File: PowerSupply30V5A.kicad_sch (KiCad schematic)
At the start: 110 parts, among them IC1 MC7805BDTRKG, IC2 MC7815BDTRKG, IC3 MC7915BD2TR4G, IC4 MC7815BDTRKG, IC5 MC7812BDTRKG, IC6 MC7805BDTRKG, IC7 MC7915BD2TR4G, IC9 MC7812BDTRKG, J1 1017503, J11 1017503, J2 1017503, J3 76825-0004, J4 39300020, J5 76825-0004, J6 1017503, J7 ${FAMILY}, J8 ${FAMILY}, Q1 IRFP460, Q3 IRFP460, T1 AVB2.3_2_15, U1 ADA4062-2ARMZ, U2 ADA4062-2ARMZ, U3 ADA4062-2ARMZ

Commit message: Added few comments for next steps
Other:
- note added: "NEXT: Power MOSFET stage-Missing calculation for rectifier: Not done for any of t Do voltage control+ V gate control phases. Remember that when sending voltage to PSU monitoring: Is better to step it up so that is no so sensible"
- note removed: "NEXT: Power MOSFET stage-Missing calculation for rectifier: Not done for any of them"
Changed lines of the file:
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@@
 		)
 	)
-	(text "NEXT: Power MOSFET stage-Missing calculation for rectifier: Not done for any of them\n"
+	(text "NEXT: Power MOSFET stage-Missing calculation for rectifier: Not done for any of t\nDo voltage control+ V gate control phases.\nRemember that when sending voltage to PSU monitoring: Is better to step it up so that is no so sensible\n\n"
 		(exclude_from_sim no)
-		(at -107.442 37.592 0)
+		(at -107.442 40.894 0)
 		(effects
 			(font

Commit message: continued adding resistors
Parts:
- removed R28: 10kΩ, m_Resistor_SMD:RESC3216X60N, symbol m_Resistor_SMD:RCA120610K0JNEASR
- added LED5, LED6, LED7, LED8: Q62702P5179, USER_LED:Q62702P5179, symbol Q62702P5179:Q62702P5179
- added R28, R35: 1.2kΩ, m_Resistor_SMD:RESC3216X60N, symbol m_Resistor_SMD:1.2k_1206_0.25W_5%
- added R29: 1kΩ, m_Resistor_SMD:RESC3216X60N, symbol m_Resistor_SMD:1k_1206_0.25W_5%
- added R33: 330Ω, Resistor_SMD:R_1218_3246Metric_Pad1.22x4.75mm_HandSolder, symbol Device:R
- added R34: 10kΩ, m_Resistor_SMD:RESC3216X60N, symbol m_Resistor_SMD:10k_1206_0.25W_5%
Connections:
- net +15V: now also R35. (2)
- net +5V: now also R33.1
- net -15V: now also R28. (2)
- net GND: now also LED5.2 (A), LED6.1 (K), LED7.2 (A), LED8.2 (A)
- net V_GATE: now also R34. (2)
- net at Q3.1: now also R34. (2)
- new net: LED8.1 (K), R33.2
- new net: LED5.1 (K), R35. (2)
- new net: LED6.2 (A), R28. (2)
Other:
- note added: "All capacitors library are missing"

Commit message: Updated voltage monitoring+voltage control , started with opamp selection
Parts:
- removed LED5, LED6, LED7, LED8: Q62702P5179, USER_LED:Q62702P5179, symbol Q62702P5179:Q62702P5179
- removed R28, R35: 1.2kΩ, m_Resistor_SMD:RESC3216X60N, symbol m_Resistor_SMD:1.2k_1206_0.25W_5%
- removed R29: 1kΩ, m_Resistor_SMD:RESC3216X60N, symbol m_Resistor_SMD:1k_1206_0.25W_5%
- removed R33: 330Ω, Resistor_SMD:R_1218_3246Metric_Pad1.22x4.75mm_HandSolder, symbol Device:R
- added D2, D3: 1N4150W-E3-18, m_Diode:SOD3716X135N, symbol m_Diode:Diode_200mA_1V
- added IC8: LF247DT, m_OpAmp:SOIC127P600X175-14N, symbol m_OpAmp:LF247DT
- added LED5, LED6, LED7, LED8: CMD15-21VGD_TR8, m_Diode_LED:LEDC3215X130N, symbol m_Diode_LED:Green_LED_20mA
- added R28, R32: 620Ω, m_Resistor_SMD:RESC3216X60N, symbol m_Resistor_SMD:620R_1206_0.25W_5%_1
- added R29: 130Ω, m_Resistor_SMD:RESC3216X60N, symbol m_Resistor_SMD:130R_1206_0.25W_5%
- added R33: 470Ω, m_Resistor_SMD:RESC3216X60N, symbol m_Resistor_SMD:470R_1206_0.25W_5%
- added R35: 10kΩ, m_Resistor_SMD:RESC3216X60N, symbol m_Resistor_SMD:10k_1206_0.25W_5%
- added Z1: 6V, m_Diode_Zener:SOD3716X135N, symbol m_Diode_Zener:MMSZ5233B-E3-08
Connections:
- net +12V: now also R33. (2), Z1.1 (K)
- net +15V: now also R28. (2)
- net +5V: now also R29. (2)
- net -15V: now also R32. (2)
- net GND: now also LED5.2 (A), LED6.1 (K), LED7.2 (A), LED8.2 (A)
- net I_control: now also D3.1 (K)
- net V_GATE: now also D2.2 (A), D3.2 (A), R35. (2)
- net V_control: now also D2.1 (K)
- new net: LED7.1 (K), R29. (2)
- new net: R35. (2), Z1.2 (A)
- new net: LED8.1 (K), R28. (2)
- new net: LED6.2 (A), R32. (2)
- new net: LED5.1 (K), R33. (2)
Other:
- note added: "(15-2,1)/(20e-3)=645 Ohm (12-2,1)/(20e-3)=495 Ohm (5-2,1)/(20e-3)=145 Ohm"
- note added: "(I_max operation in diodes: 6V/10kOhm=0.6mA)"
- note added: "If=200mA Vf=1V"
- note added: "If=20mA Vf=2.1V"
- note added: "NEXT:Next I_control+ V_control+ Buffer NEXT (X2): Consider which voltage I want to send to the PSU_Monitoring board: In case I need to change something Remember that when sending voltage to PSU monitoring: Is better to step it up so that is no so sensible"
- note added: "Todo estoy diseñando en paquete 1206 :) Standard: Asi puedo tener elementos guardados"
- note added: "Una vez terminado: Hacer check electrico del esquematico+ actualizar numeros"
- note removed: "NEXT: Power MOSFET stage-Missing calculation for rectifier: Not done for any of t Do voltage control+ V gate control phases. Remember that when sending voltage to PSU monitoring: Is better to step it up so that is no so sensible"
- moved on the sheet: C23, C24, IC1, TP13

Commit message: Added control
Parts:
- removed IC8: LF247DT, m_OpAmp:SOIC127P600X175-14N, symbol m_OpAmp:LF247DT
- removed R30: FCSL76R050DER, m_Resistor_measurement:RESC3876X70N, symbol m_Resistor_measurement:FCSL76R050DER
- added C29, C32, C34, C36: 0.1uF, Capacitor_SMD:C_1206_3216Metric_Pad1.33x1.80mm_HandSolder, symbol Device:C
- added C30, C31: 1uF, Capacitor_SMD:C_1206_3216Metric_Pad1.33x1.80mm_HandSolder, symbol Device:C
- added C33, C35: 4.7nF, Capacitor_SMD:C_1206_3216Metric_Pad1.33x1.80mm_HandSolder, symbol Device:C
- added IC8: LF247DT, m_OpAmp:SOIC127P600X175-14N, symbol m_OpAmp:LF247DT_symbol_modified
- added R30, R36, R38, R44: 10kΩ, m_Resistor_SMD:RESC3216X60N, symbol m_Resistor_SMD:10k_1206_0.25W_5%
- added R31: FCSL76R050DER, m_Resistor_measurement:RESC3876X70N, symbol m_Resistor_measurement:FCSL76R050DER
- added R37, R43: 180kΩ, m_Resistor_SMD:RESC3216X60N, symbol m_Resistor_SMD:180k_1206_0.25W_5%
- added R39, R40, R41, R45, R46, R53, R54, R55: 100kΩ, m_Resistor_SMD:RESC3216X60N, symbol m_Resistor_SMD:100k_1206_0.25W_5%
- added R42: 22kΩ, m_Resistor_SMD:RESC3216X60N, symbol m_Resistor_SMD:22k_1206_0.25W_5%
- added R47, R48: 8.2kΩ, m_Resistor_SMD:RESC3216X60N, symbol m_Resistor_SMD:8.2k_1206_0.25W_5%
- added R49, R51: 18kΩ, m_Resistor_SMD:RESC3216X60N, symbol m_Resistor_SMD:18k_1206_0.25W_5%_1
- added R50, R52: 0Ω, m_Resistor_SMD:RESC3216X60N, symbol m_Resistor_SMD:0R_1206_0.25W_5%_1
- added R56: 100Ω, m_Resistor_SMD:RESC3216X60N, symbol m_Resistor_SMD:100R_1206_0.25W_5%_1
- C21: footprint Capacitor_SMD:C_0805_2012Metric_Pad1.18x1.45mm_HandSolder -> Capacitor_SMD:C_1206_3216Metric_Pad1.33x1.80mm_HandSolder
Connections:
- net +15V: now also C29.1, C30.1, IC8.4 (V+)
- net -15V: now also C31.1, C32.1, IC8.11 (V-)
- net 0V_IN: now also C34.1, R45. (2)
- net GND: now also C29.2, C30.2, C31.2, C32.2, R30. (2), R31.1, R42. (2), R43. (2), R52. (2), R56. (2)
- net I_OUT_MEAS-: now also R31.2, R36. (2), R46. (2)
- net I_REFERENCE: now also R40. (2)
- net I_control: now also C33.1, IC8.8, R41. (2)
- net V_REFERENCE: now also R54. (2)
- net V_control: now also C35.1, IC8.14, R55. (2)
- new net: IC8.1, R38. (2), R39. (2)
- new net: R37. (2), R38. (2)
- new net: C36.1, IC8.7, R50. (2), R53. (2)
- new net: R49. (2), R50. (2)
- new net: C35.2, IC8.13 (-), R55. (2), R56. (2)
- new net: IC8.10 (+), R39. (2), R40. (2)
- new net: C36.2, IC8.12 (+), R53. (2), R54. (2)
- new net: IC8.2 (-), R36. (2), R37. (2)
- new net: IC8.3 (+), R30. (2), R44. (2)
- new net: C34.2, IC8.5 (+), R47. (2), R51. (2)
- new net: IC8.6 (-), R48. (2), R49. (2)
- new net: C33.2, IC8.9 (-), R41. (2), R42. (2)
- new net: R46. (2), R48. (2)
- new net: R43. (2), R44. (2)
- new net: R51. (2), R52. (2)
- new net: R45. (2), R47. (2)
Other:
- note added: "0/5V"
- note added: "Add testpoints"
- note added: "All capacitors library are missing: I need to replace both electrolitic and ceramic ones"
- note added: "Current integrator"
- note added: "Current sensing"
- note added: "Gain=0.167 IN:(0/30) OUT:(0/-5V)"
- note added: "Gain=20 IN:(0/0.25V[5A*50mOhm]) OUT:(0/-5V)"
- note added: "This instead of sending measurement raw from the output, I can send the one from the opamp, that is already between 0/-5V"
- note added: "Voltage integrator"
- note added: "Voltage sensing"
- note removed: "All capacitors library are missing"

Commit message: Updated comments
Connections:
- new net: IC8.1, R38. (2), R39. (2)
- new net: IC8.3 (+), R30. (2), R44. (2)
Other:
- note added: "NEXT (X2): Consider which voltage I want to send to the PSU_Monitoring board: In case I need to change something Remember that when sending voltage to PSU monitoring: Is better to step it up so that is no so sensible"
- note removed: "NEXT:Next I_control+ V_control+ Buffer NEXT (X2): Consider which voltage I want to send to the PSU_Monitoring board: In case I need to change something Remember that when sending voltage to PSU monitoring: Is better to step it up so that is no so sensible"
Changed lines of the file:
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@@
 		)
 	)
-	(text "NEXT:Next I_control+ V_control+ Buffer\nNEXT (X2): Consider which voltage I want to send to the PSU_Monitoring board: In case I need to change something\nRemember that when sending voltage to PSU monitoring: Is better to step it up so that is no so sensible\n\n"
-		(exclude_from_sim no)
-		(at -107.442 40.894 0)
+	(text "NEXT (X2): Consider which voltage I want to send to the PSU_Monitoring board: In case I need to change something\nRemember that when sending voltage to PSU monitoring: Is better to step it up so that is no so sensible\n\n"
+		(exclude_from_sim no)
+		(at -106.68 43.434 0)
 		(effects
 			(font
@@
 	(text "Add testpoints"
 		(exclude_from_sim no)
-		(at -98.044 76.2 0)
-		(effects
-			(font
+		(at -100.076 50.292 0)
+		(effects
+			(font

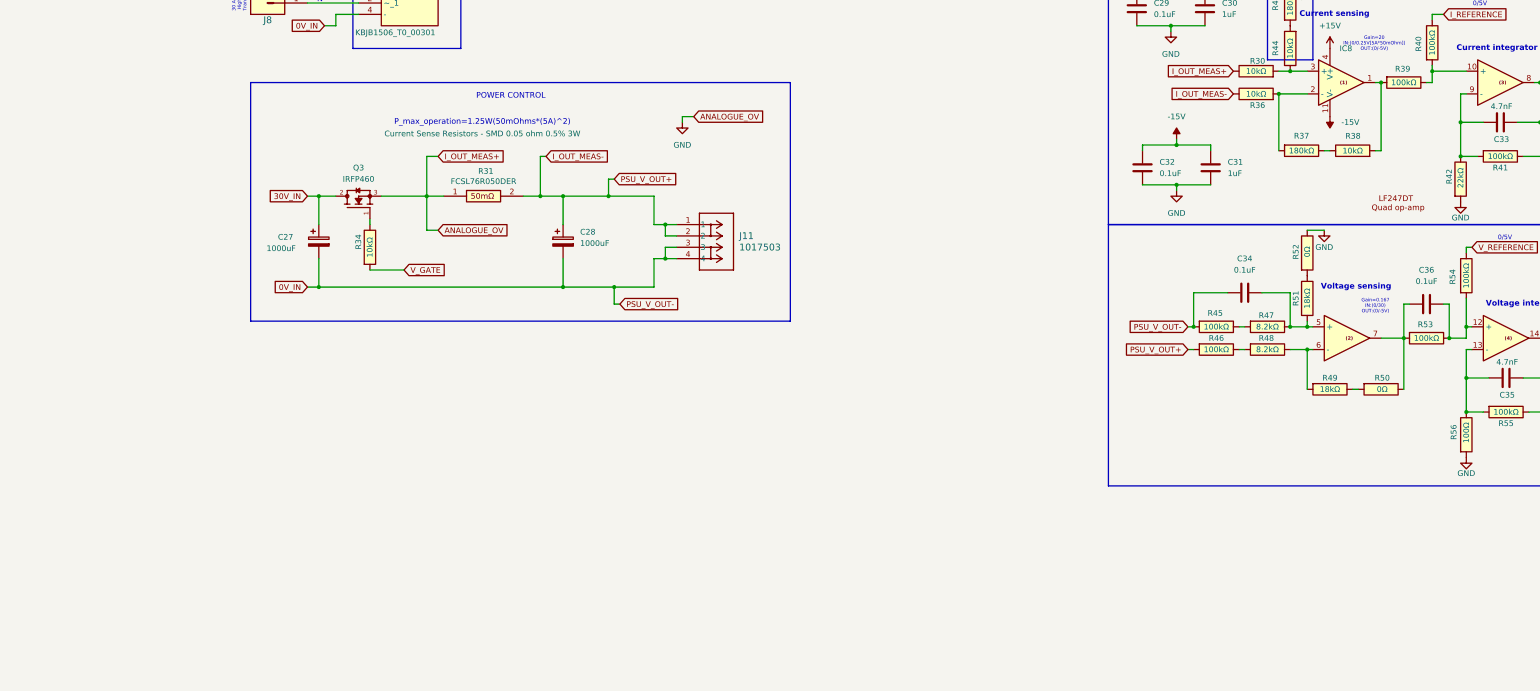
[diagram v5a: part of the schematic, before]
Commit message: Started thinking about sending measurement to PSU_monitoring PCB
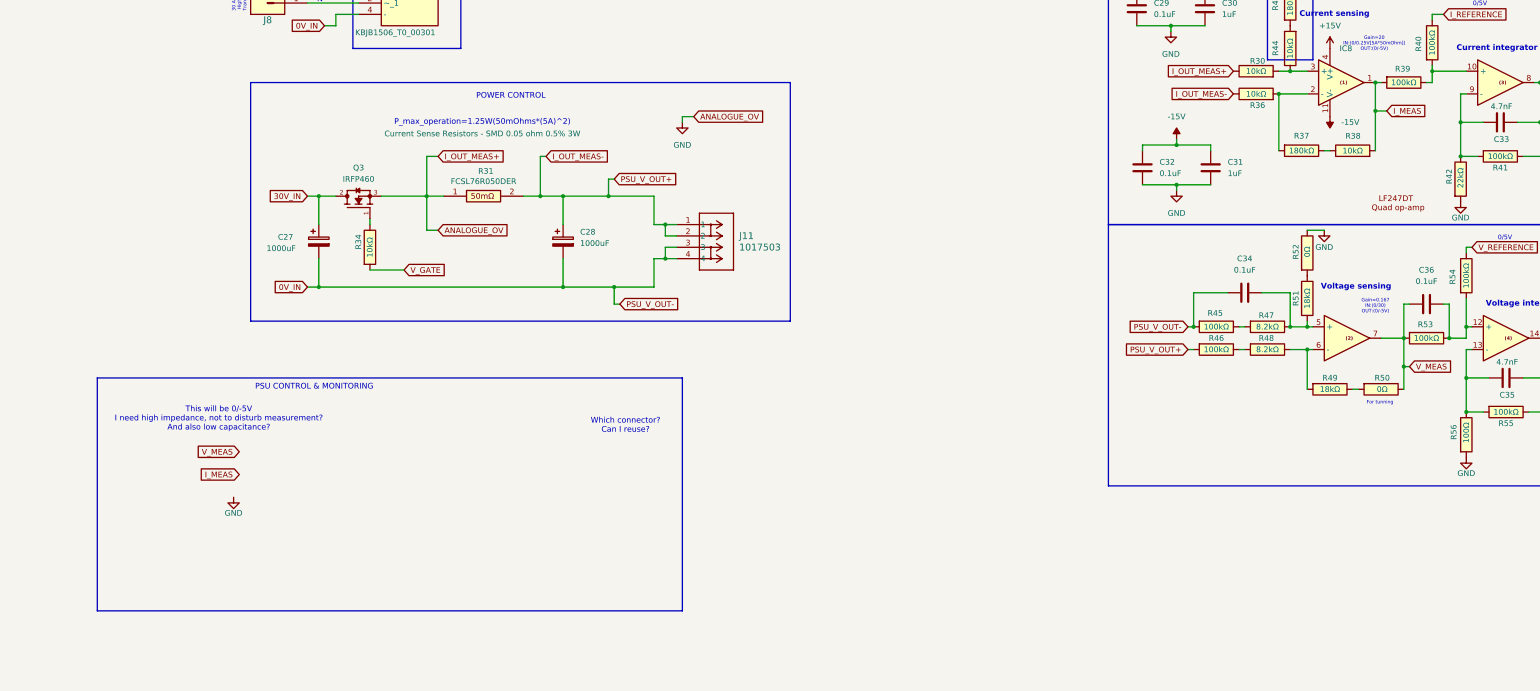
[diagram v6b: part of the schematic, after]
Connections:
- net I_MEAS: now reaches IC8.1, R38. (2), R39. (2)
- net at R37. (2): now also IC8.2 (-), R36. (2); no longer R38. (2)
- net V_MEAS: now reaches C36.1, IC8.7, R50. (2), R53. (2)
- net at R49. (2): now also IC8.6 (-), R48. (2); no longer R50. (2)
- new net: R37. (2), R38. (2)
- new net: R49. (2), R50. (2)
- new net: IC8.10 (+), R39. (2), R40. (2)
- new net: IC8.3 (+), R30. (2), R44. (2)
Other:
- note added: "For tunning"
- note added: "This will be 0/-5V I need high impedance, not to disturb measurement? And also low capacitance?"
- note added: "Which connector? Can I reuse?"

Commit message: Finished reference +measurement buffers+fan--> next step: power from trafo+rectifier calculate
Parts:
- added IC10: LF247DT, m_OpAmp:SOIC127P600X175-14N, symbol m_OpAmp:LF247DT_symbol_modified
- added J10, J9: 1755752, m_Connectors:1755752, symbol m_Connectors:1755752
- added J12: ${FAMILY}, PHOENIX THD:PHOENIX_1755736, symbol Connectors:Connector 2 Male
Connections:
- net +12V: now also J12.1
- net +15V: now also IC10.4 (V+)
- net +5V: now also J9.4
- net -15V: now also IC10.11 (V-)
- net GND: now also J10.2, J10.4, J12.2, J9.1
- net I_MEAS: now also IC10.10 (+)
- net I_REFERENCE: now also IC10.1, IC10.2 (-)
- net V_MEAS: now also IC10.12 (+)
- net V_REFERENCE: now also IC10.6 (-), IC10.7
- net at R37. (2): now also IC8.2 (-), R36. (2); no longer R38. (2)
- net at R49. (2): now also IC8.6 (-), R48. (2); no longer R50. (2)
- new net: R37. (2), R38. (2)
- new net: R49. (2), R50. (2)
- new net: IC10.8, IC10.9 (-), J10.1
- new net: IC10.13 (-), IC10.14, J10.3
- new net: IC8.10 (+), R39. (2), R40. (2)
- new net: IC8.3 (+), R30. (2), R44. (2)
- new net: IC10.3 (+), J9.3
- new net: IC10.5 (+), J9.2
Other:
- note added: "(I send the 5V to work with potentiometer before designing the PSU Montiring PCB)"
- note added: "0/-5V"
- note added: "NEXT(X2): Capacitor library+ Electrical check +testpoints"
- note added: "NEXT: Calculate power needed by LDO: Decide with transformer I need and also which (two) bridge rectifier I need"
- note added: "PSU CONTROL & MONITORING (Sending signals to PSU Monitoring PCB)"
- note added: "Voltage buffer for the measurements. I need high input impedance from the voltage measurement"
- note added: "Voltage buffer for the references. I need low output impedance from the voltage sources"
- note removed: "NEXT (X2): Consider which voltage I want to send to the PSU_Monitoring board: In case I need to change something Remember that when sending voltage to PSU monitoring: Is better to step it up so that is no so sensible"
- note removed: "This will be 0/-5V I need high impedance, not to disturb measurement? And also low capacitance?"
- note removed: "Todo estoy diseñando en paquete 1206 :) Standard: Asi puedo tener elementos guardados"
- note removed: "Which connector? Can I reuse?"
- moved on the sheet: BR4, C27, C28, J11, J8, Q3, R31, R34

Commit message: Added 1uF capacitors, change the rest of capacitor by copy pasting (like done for resistors
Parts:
- removed C21, C22, C24, C26, C30, C31: 1uF, Capacitor_SMD:C_1206_3216Metric_Pad1.33x1.80mm_HandSolder, symbol Device:C
- added C21, C22, C24, C30, C31, C37: 1μF_25V, m_Capacitor_ceramic_SMD:CAPC2012X94N, symbol m_Capacitor_ceramic_SMD:0805_1μF_25V_20%
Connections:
- net +12V: now also C24. (2)
- net +15V: now also C30. (2), C37. (2)
- net +5V: now also C22. (2)
- net -15V: now also C21. (2), C31. (2)
- net GND: now also C21. (2), C22. (2), C24. (2), C30. (2), C31. (2), C37. (2)
- net at R37. (2): now also IC8.2 (-), R36. (2); no longer R38. (2)
- net at R49. (2): now also IC8.6 (-), R48. (2); no longer R50. (2)
- new net: R37. (2), R38. (2)
- new net: R49. (2), R50. (2)
- new net: IC8.10 (+), R39. (2), R40. (2)
- new net: IC8.3 (+), R30. (2), R44. (2)
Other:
- note added: "Could it be that capacitors where 25V instead of 50V?> This time I will select 50V, because I want to have them standard at home"
- note added: "NEXT: 1uF changed , add other values by copy pasting Capacitor select 1206 (Correccion, no tiene sentido que todos sean iguales) Lo que puedo encontrar es un kit ya preparado (Y comprar una vez:) Luego contemplar si deberia de hacer lo mismo con las resistencias https://www.mouser.co.uk/en/ProductDetail/Wurth-Elektronik/885070?qs=%252BUQ4csG8RsciqaV%252BTbV4fQ%3D%3D"
